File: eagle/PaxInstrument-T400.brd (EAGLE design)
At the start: 99.1 x 50.8 mm, 115 parts, among them IC1 MCP3424, J1 MICRO-SDCARD-CONNECTOR-330006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, U1 MCP9800, U3 MCP73831, U4 MIC5219-3.3V, U8 NC7S32, X1 FH12-12S-0.5SH, Y1 RESONATORSMD

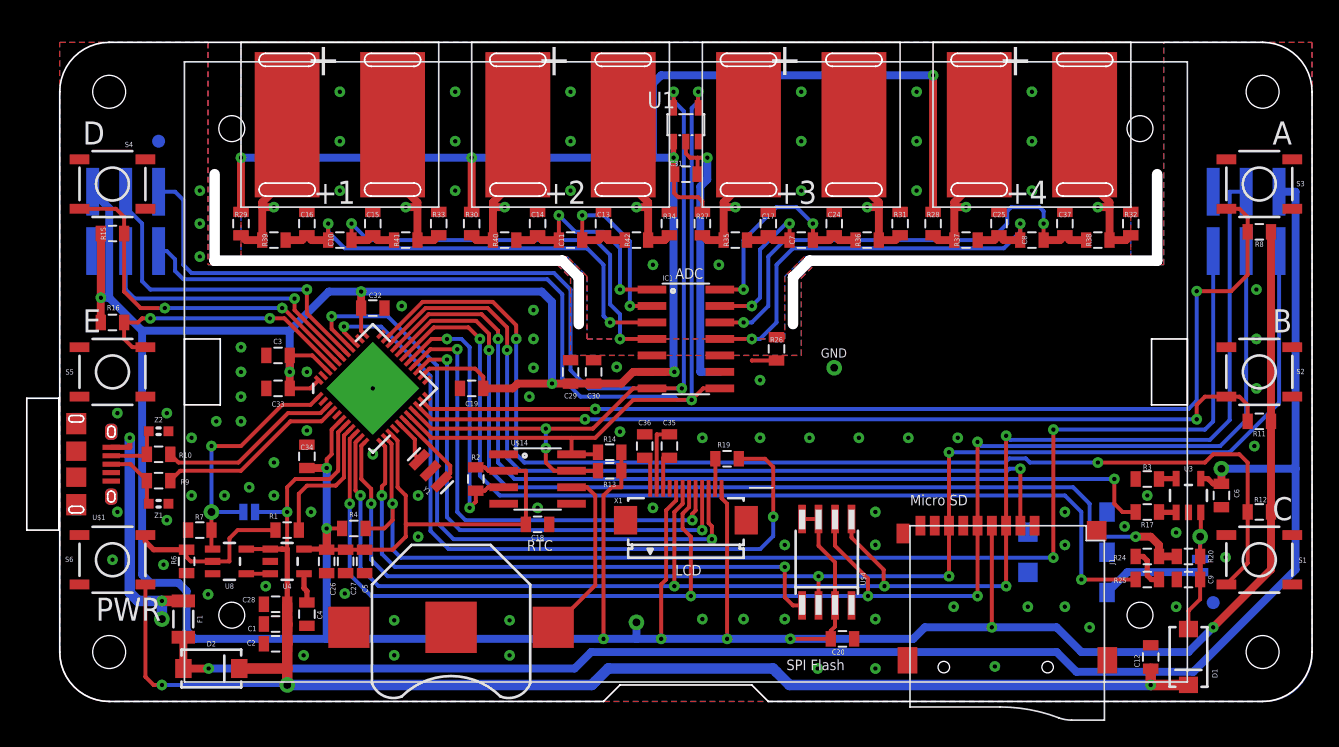
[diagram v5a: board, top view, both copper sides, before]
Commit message: Remove fiducials for Rev 0.10
Fix issue Remove fiducials #125
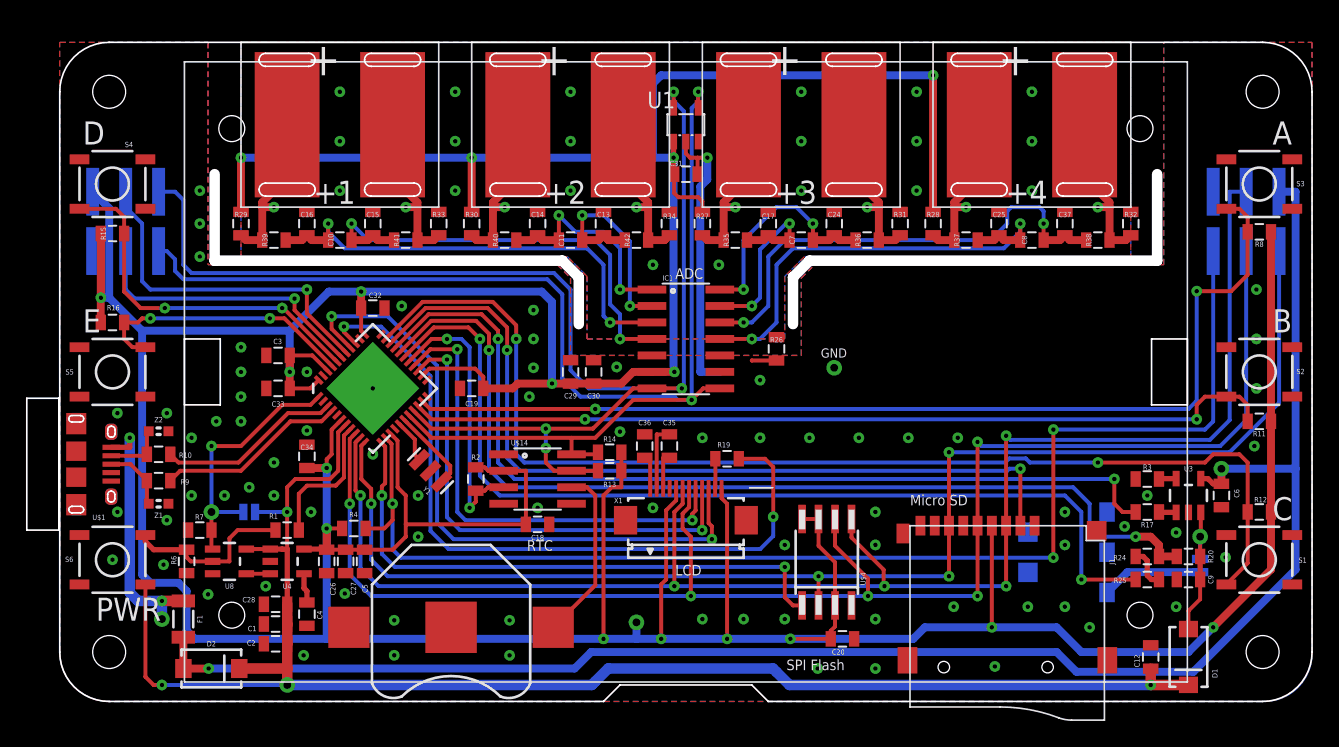
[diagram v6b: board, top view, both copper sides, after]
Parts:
- removed FID1, FID2: FIDUCIAL1X2, SparkFun-Aesthetics:FIDUCIAL-1X2
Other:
- board text removed: "(0.3,0.3)"
- board text removed: "(3.5,1.7)"
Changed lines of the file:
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@@
 <grid distance="25" unitdist="mil" unit="mm" style="lines" multiple="1" display="yes" altdistance="6.25" altunitdist="mil" altunit="mil"/>
 <layers>
-<layer number="1" name="Top" color="4" fill="1" visible="yes" active="yes"/>
+<layer number="1" name="Top" color="4" fill="1" visible="no" active="yes"/>
 <layer number="2" name="Route2" color="1" fill="3" visible="no" active="no"/>
 <layer number="3" name="Route3" color="4" fill="3" visible="no" active="no"/>
@@
 <dimension x1="0" y1="-3.81" x2="7.62" y2="-3.81" x3="3.81" y3="-15.24" textsize="1.778" layer="47"/>
 <dimension x1="-10.16" y1="0" x2="-10.16" y2="7.62" x3="-11.43" y3="3.81" textsize="1.778" layer="47"/>
-<text x="88.9" y="6.35" size="0.635" layer="22" font="vector" ratio="15" rot="MR0" align="center">(0.3,0.3)</text>
-<text x="7.62" y="44.45" size="0.635" layer="22" font="vector" ratio="15" rot="MR0" align="center">(3.5,1.7)</text>
 <dimension x1="5.08" y1="54.61" x2="91.44" y2="54.61" x3="48.26" y3="62.23" textsize="1.778" layer="47" unit="inch"/>
 <dimension x1="100.33" y1="25.4" x2="100.33" y2="18.796" x3="103.124" y3="22.098" textsize="1.778" layer="47" unit="inch"/>
@@
 <attribute name="NAME" x="81.7245" y="9.3345" size="0.4064" layer="25" rot="R180" align="center"/>
 </element>
-<element name="FID1" library="SparkFun-Aesthetics" package="FIDUCIAL-1X2" value="FIDUCIAL1X2" x="88.9" y="7.62" smashed="yes" rot="MR0">
-<attribute name="MPN" value="N/A" x="88.9" y="7.62" size="1.778" layer="28" rot="MR0" display="off"/>
-<attribute name="OC_DIGIKEY" value="N/A" x="88.9" y="7.62" size="1.778" layer="28" rot="MR0" display="off"/>
-</element>
-<element name="FID2" library="SparkFun-Aesthetics" package="FIDUCIAL-1X2" value="FIDUCIAL1X2" x="7.62" y="43.18" smashed="yes" rot="MR0">
-<attribute name="MPN" value="N/A" x="7.62" y="43.18" size="1.778" layer="28" rot="MR0" display="off"/>
-<attribute name="OC_DIGIKEY" value="N/A" x="7.62" y="43.18" size="1.778" layer="28" rot="MR0" display="off"/>
-</element>
 <element name="U$1" library="blinkinlabs" package="USB_MICRO_THRUHOLE" value="USB_MICROSMT+THRUHULE" x="1.27" y="18.288" locked="yes" smashed="yes" rot="R270">

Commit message: Changed Longer soler pads on 2x3 header footprint for Rev 0.10
Changed Longer soler pads on 2x3 header footprint #122
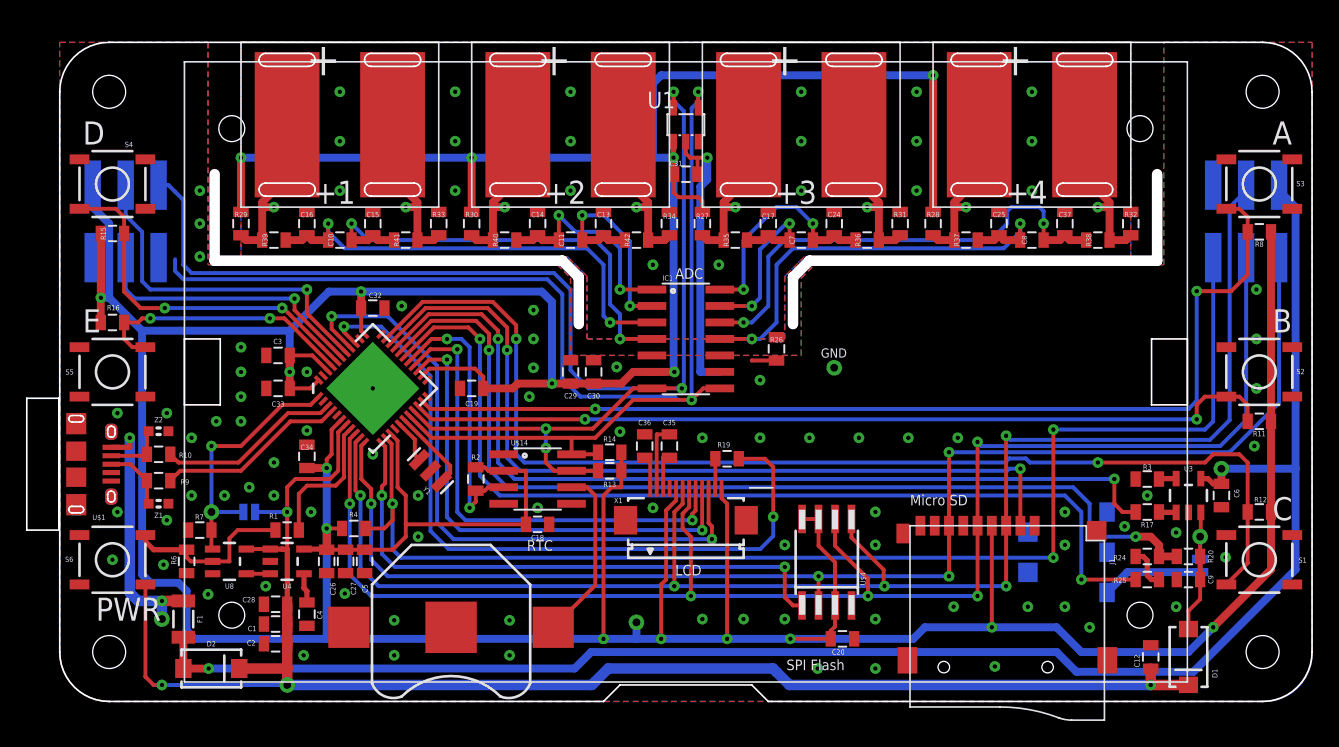
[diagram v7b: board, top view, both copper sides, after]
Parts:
- ICSP, ICSP1: device SparkFun-Connectors:2X3_SMT_POSTS -> PaxInstrument-T400:SPARKFUN-CONNECTORS_2X3_SMT_POSTS_PAXINSTRUMENT
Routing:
- net SCL: track 105.0 -> 103.5 mm
- net SCK: track 122.5 -> 122.0 mm
- net RESET: track 99.2 -> 98.7 mm
- net MISO: track 105.0 -> 104.5 mm
- net DATA2: track 22.3 -> 21.8 mm
- net DATA1: track 26.5 -> 27.0 mm
- net 3.3V: track 462.7 -> 463.2 mm
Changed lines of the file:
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@@
 <setting verticaltext="up"/>
 </settings>
-<grid distance="25" unitdist="mil" unit="mm" style="lines" multiple="1" display="yes" altdistance="6.25" altunitdist="mil" altunit="mil"/>
+<grid distance="25" unitdist="mil" unit="mil" style="lines" multiple="1" display="yes" altdistance="6.25" altunitdist="mil" altunit="mil"/>
 <layers>
 <layer number="1" name="Top" color="4" fill="1" visible="no" active="yes"/>
@@
 </autorouter>
 <elements>
-<element name="ICSP" library="SparkFun-Connectors" package="2X3_SMT_POSTS" value="ICSP" x="91.44" y="37" smashed="yes" rot="MR0">
-<attribute name="PROD_ID" value="CONN-11415" x="91.44" y="37" size="1.778" layer="28" rot="MR0" display="off"/>
+<element name="ICSP" library="PaxInstrument-T400" package="SPARKFUN-CONNECTORS_2X3_SMT_POSTS_PAXINSTRUMENT" value="ICSP" x="91.44" y="37" smashed="yes" rot="MR0">
 <attribute name="MPN" value="95278-101A06LF" x="91.44" y="37" size="1.778" layer="28" rot="MR0" display="off"/>
 <attribute name="OC_DIGIKEY" value="609-3487-2-ND" x="91.44" y="37" size="1.778" layer="28" rot="MR0" display="off"/>
@@
 <attribute name="NAME" x="16.47825" y="14.2875" size="0.4064" layer="25" align="center"/>
 </element>
-<element name="ICSP1" library="SparkFun-Connectors" package="2X3_SMT_POSTS" value="ICSP" x="5.08" y="37" smashed="yes" rot="MR0">
-<attribute name="PROD_ID" value="CONN-11415" x="5.08" y="37" size="1.778" layer="28" font="vector" ratio="15" rot="MR0" display="off"/>
+<element name="ICSP1" library="PaxInstrument-T400" package="SPARKFUN-CONNECTORS_2X3_SMT_POSTS_PAXINSTRUMENT" value="ICSP" x="5.08" y="37" smashed="yes" rot="MR0">
 <attribute name="MPN" value="95278-101A06LF" x="5.08" y="37" size="1.778" layer="28" rot="MR0" display="off"/>
 <attribute name="OC_DIGIKEY" value="609-3487-2-ND" x="5.08" y="37" size="1.778" layer="28" rot="MR0" display="off"/>
@@
 <wire x1="25.019" y1="13.335" x2="25.654" y2="13.97" width="0.3048" layer="1"/>
 <wire x1="25.654" y1="13.97" x2="25.654" y2="15.24" width="0.3048" layer="1"/>
-<wire x1="88.9" y1="34.714" x2="88.9" y2="21.59" width="0.3048" layer="16"/>
+<wire x1="88.9" y1="34.206" x2="88.9" y2="21.59" width="0.3048" layer="16"/>
 <wire x1="88.9" y1="21.59" x2="88.265" y2="20.955" width="0.3048" layer="16"/>
 <wire x1="88.265" y1="20.955" x2="76.581" y2="20.955" width="0.3048" layer="16"/>
@@
 <wire x1="41.3275" y1="19.05" x2="39.4462" y2="19.05" width="0.3048" layer="1"/>
 <wire x1="38.735" y1="31.385" x2="37.57625" y2="32.54375" width="0.3048" layer="16"/>
-<wire x1="7.62" y1="34.714" x2="8.255" y2="34.714" width="0.3048" layer="16"/>
-<wire x1="8.255" y1="34.714" x2="8.89" y2="34.079" width="0.3048" layer="16"/>
+<wire x1="8.89" y1="34.079" x2="7.62" y2="34.206" width="0" layer="19" extent="16-16"/>
 </signal>
 <signal name="SDA">
@@
 <wire x1="44.196" y1="24.13" x2="41.093103125" y2="21.027103125" width="0.3048" layer="1"/>
 <contactref element="ICSP1" pad="2"/>
-<wire x1="7.62" y1="39.286" x2="8.89" y2="39.286" width="0.3048" layer="16"/>
-<wire x1="8.89" y1="39.286" x2="9.525" y2="38.651" width="0.3048" layer="16"/>
+<wire x1="8.89" y1="39.286" x2="9.483" y2="38.693" width="0.3048" layer="16"/>
+<wire x1="9.483" y1="38.693" x2="9.525" y2="38.651" width="0.3048" layer="16"/>
 <wire x1="9.525" y1="38.651" x2="9.525" y2="33.655" width="0.3048" layer="16"/>
 <wire x1="9.525" y1="33.655" x2="10.16" y2="33.02" width="0.3048" layer="16"/>
@@
 <wire x1="37.465" y1="18.415" x2="38.1" y2="17.78" width="0.3048" layer="1"/>
 <wire x1="38.1" y1="17.78" x2="39.4462" y2="17.78" width="0.3048" layer="1"/>
+<wire x1="7.62" y1="39.794" x2="8.382" y2="39.794" width="0.3048" layer="16"/>
+<wire x1="8.382" y1="39.794" x2="8.89" y2="39.286" width="0.3048" layer="16"/>
 </signal>
 <signal name="3.3V">
@@
 <wire x1="26.67" y1="12.7" x2="26.67" y2="13.6525" width="0.3048" layer="1"/>
 <wire x1="41.148" y1="24.5" x2="39.37" y2="24.5" width="0.6096" layer="1"/>
-<wire x1="2.54" y1="39.286" x2="3.81" y2="38.016" width="0.6096" layer="16"/>
-<wire x1="3.81" y1="38.016" x2="3.81" y2="31.115" width="0.6096" layer="16"/>
 <wire x1="3.164" y1="36.068" x2="3.164" y2="29.21" width="0.6096" layer="1"/>
 <wire x1="3.164" y1="36.195" x2="3.175" y2="36.184" width="0.6096" layer="1"/>
@@
 <wire x1="47.31" y1="41.91" x2="47.31" y2="40.69" width="0.4064" layer="1"/>
 <wire x1="47.31" y1="40.69" x2="47.36" y2="40.64" width="0.4064" layer="1"/>
+<wire x1="2.54" y1="39.794" x2="2.54" y2="38.1" width="0.6096" layer="16"/>
+<wire x1="2.54" y1="38.1" x2="3.81" y2="36.83" width="0.6096" layer="16"/>
+<wire x1="3.81" y1="36.83" x2="3.81" y2="31.115" width="0.6096" layer="16"/>
 </signal>
 <signal name="3V3EN">
@@
 <contactref element="J1" pad="7"/>
 <wire x1="68.539" y1="9.652" x2="68.539" y2="13.546" width="0.3048" layer="1"/>
-<wire x1="93.98" y1="34.714" x2="93.98" y2="23.01875" width="0.3048" layer="16"/>
+<wire x1="93.98" y1="34.206" x2="93.98" y2="23.01875" width="0.3048" layer="16"/>
 <wire x1="93.98" y1="23.01875" x2="90.17" y2="19.20875" width="0.3048" layer="16"/>
 <wire x1="90.17" y1="19.20875" x2="68.539" y2="19.20875" width="0.3048" layer="16"/>
@@
 <wire x1="72.939" y1="8.89" x2="72.939" y2="13.546" width="0.3048" layer="1"/>
 <via x="63.5635" y="8.89" extent="1-16" drill="0.3302"/>
-<wire x1="91.44" y1="39.286" x2="90.17" y2="39.286" width="0.3048" layer="16"/>
-<wire x1="90.17" y1="39.286" x2="90.17" y2="21.68525" width="0.3048" layer="16"/>
+<wire x1="90.17" y1="38.1" x2="90.17" y2="21.68525" width="0.3048" layer="16"/>
 <wire x1="90.17" y1="21.68525" x2="88.646" y2="20.16125" width="0.3048" layer="16"/>
 <wire x1="88.646" y1="20.16125" x2="73.2565" y2="20.16125" width="0.3048" layer="16"/>
@@
 <wire x1="61.0235" y1="14.0615" x2="61.0235" y2="12.6365" width="0.3048" layer="1"/>
 <wire x1="61.0235" y1="12.6365" x2="63.5" y2="10.16" width="0.3048" layer="1"/>
+<wire x1="91.44" y1="39.794" x2="91.44" y2="39.37" width="0.3048" layer="16"/>
+<wire x1="91.44" y1="39.37" x2="90.17" y2="38.1" width="0.3048" layer="16"/>
 </signal>
 <signal name="SCK">
@@
 <wire x1="70.739" y1="8.128" x2="70.739" y2="13.546" width="0.3048" layer="1"/>
 <via x="62.2935" y="8.128" extent="1-16" drill="0.3302"/>
-<wire x1="91.44" y1="34.714" x2="91.44" y2="21.685" width="0.3048" layer="16"/>
+<wire x1="91.44" y1="34.206" x2="91.44" y2="21.685" width="0.3048" layer="16"/>
 <wire x1="91.44" y1="21.685" x2="89.44" y2="19.685" width="0.3048" layer="16"/>
 <wire x1="89.44" y1="19.685" x2="71.0565" y2="19.685" width="0.3048" layer="16"/>
@@
 <contactref element="GND" pad="39"/>
 <via x="18.0975" y="31.0515" extent="1-16" drill="0.3302"/>
-<wire x1="5.08" y1="31.75" x2="5.08" y2="34.714" width="0.3048" layer="16"/>
+<wire x1="5.08" y1="31.75" x2="5.08" y2="34.206" width="0.3048" layer="16"/>
 <wire x1="18.0975" y1="31.0515" x2="5.7785" y2="31.0515" width="0.3048" layer="16"/>
 <wire x1="5.7785" y1="31.0515" x2="5.08" y2="31.75" width="0.3048" layer="16"/>
@@
 <signal name="DATA1">
 <contactref element="ICSP1" pad="4"/>
-<wire x1="5.08" y1="39.286" x2="5.08" y2="38.1" width="0.3048" layer="16"/>
-<wire x1="5.08" y1="38.1" x2="6.35" y2="36.83" width="0.3048" layer="16"/>
 <contactref element="GND" pad="38"/>
 <via x="19.05" y="31.75" extent="1-16" drill="0.3302"/>
-<wire x1="6.35" y1="32.385" x2="6.35" y2="36.83" width="0.3048" layer="16"/>
+<wire x1="6.35" y1="32.385" x2="6.35" y2="36.195" width="0.3048" layer="16"/>
 <wire x1="19.05" y1="31.75" x2="6.985" y2="31.75" width="0.3048" layer="16"/>
 <wire x1="6.985" y1="31.75" x2="6.35" y2="32.385" width="0.3048" layer="16"/>
 <wire x1="22.0793875" y1="26.887715625" x2="19.05" y2="29.917103125" width="0.3048" layer="1"/>
 <wire x1="19.05" y1="29.917103125" x2="19.05" y2="31.75" width="0.3048" layer="1"/>
+<wire x1="5.08" y1="39.794" x2="5.08" y2="37.465" width="0.3048" layer="16"/>
+<wire x1="5.08" y1="37.465" x2="6.35" y2="36.195" width="0.3048" layer="16"/>
 </signal>
 <signal name="VBUS_IN">
@@
 <wire x1="87.945" y1="17.1751" x2="88.4889" y2="17.1751" width="0.4064" layer="1"/>
 <wire x1="89.535" y1="17.93875" x2="89.535" y2="16.775" width="0.6096" layer="1"/>
-<wire x1="95.25" y1="17.93875" x2="95.25" y2="39.286" width="0.6096" layer="16"/>
-<wire x1="93.98" y1="39.286" x2="95.25" y2="39.286" width="0.6096" layer="16"/>
+<wire x1="95.25" y1="17.93875" x2="95.25" y2="38.1" width="0.6096" layer="16"/>
 <wire x1="87.376" y1="2.286" x2="95.25" y2="10.16" width="0.6096" layer="16"/>
 <wire x1="95.25" y1="10.16" x2="95.25" y2="17.93875" width="0.6096" layer="16"/>
@@
 <wire x1="76.835" y1="3.81" x2="78.359" y2="2.286" width="0.6096" layer="16"/>
 <wire x1="78.359" y1="2.286" x2="87.376" y2="2.286" width="0.6096" layer="16"/>
+<wire x1="93.98" y1="39.794" x2="93.98" y2="39.37" width="0.6096" layer="16"/>
+<wire x1="93.98" y1="39.37" x2="95.25" y2="38.1" width="0.6096" layer="16"/>
 </signal>
 <signal name="N$27">

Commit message: Switch to 0603
Switch to 0603 #121
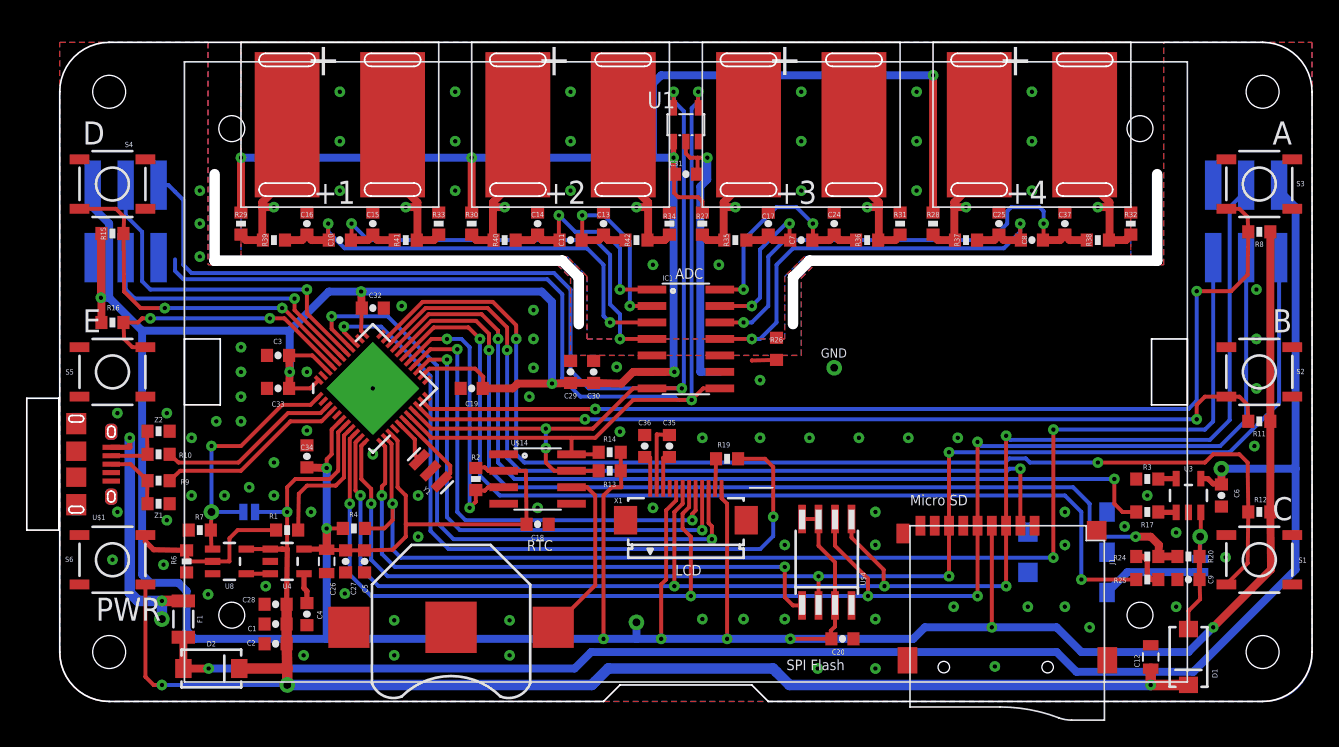
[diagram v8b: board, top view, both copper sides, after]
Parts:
- C1, C10, C11, C13, C14, C15, C16, C17, C18, C19, C2, C20, C24, C25, C27, C28, C29, C3, C30, C31, C32, C33, C34, C35, C36, C37, C4, C5, C6, C7, C8, C9: device SparkFun-Passives:0805 -> PaxInstrument-T400:SPARKFUN-CAPACITORS_0603-CAP
- C12, C26: device SparkFun-Passives:0805 -> PaxInstrument-T400:SPARKFUN-CAPACITORS_0805
- R1, R10, R11, R12, R13, R14, R15, R16, R17, R19, R2, R20, R24, R25, R27, R28, R29, R3, R30, R31, R32, R33, R34, R35, R36, R37, R38, R39, R4, R40, R41, R42, R6, R7, R8, R9: device SparkFun-Passives:0805 -> PaxInstrument-T400:SPARKFUN-RESISTORS_0603-RES
- R26: value 10k -> 150R; device SparkFun-Passives:0805 -> PaxInstrument-T400:0603
- Z1, Z2: device freetronics-master-v1.1:0603 -> PaxInstrument-T400:SPARKFUN-RESISTORS_0603-RES
